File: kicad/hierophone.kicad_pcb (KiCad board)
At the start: 2 copper layers, 220 x 130 mm, 165 parts, among them J1 AudioJack2_SwitchT, J10 Conn_01x02, J2 AudioJack2_SwitchT, J3 Conn_01x03_Pin, J4 AudioJack2_SwitchT, J5 AudioJack2_SwitchT, J6 AudioJack2_SwitchT, J7 AudioJack2_SwitchT, J8 Conn_01x02, J9 Conn_01x02, Q1 2N3904, Q2 2N3906, Q3 2N3906, SW1 SW_SPDT, SW3 SW_SPDT, U10 TL072, U11 TL072, U12 TL072, U13 TL072, U2 LM13700, U3 LM13700, U4 TL072, U5 TL072, U6 LM386, U7 NE5534, U8 TL072, U9 ICL7660

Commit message: Fixing issues with the inputs
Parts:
- removed R18: 47k, Rumblesan_Standard_Parts:R_Axial_DIN0207_L6.3mm_D2.5mm_P10.16mm_Horizontal
- removed U11: TL072, Package_DIP:DIP-8_W7.62mm_Socket
- added C44: 22pF, Rumblesan_Standard_Parts:C_Rect_L7.0mm_W2.5mm_P5.00mm, F.Cu at (76.5, 97.8)
- added R59: 100k, Rumblesan_Standard_Parts:R_Axial_DIN0207_L6.3mm_D2.5mm_P10.16mm_Horizontal, F.Cu at (52.3, 144.8)
- added R60: 100k, Rumblesan_Standard_Parts:R_Axial_DIN0207_L6.3mm_D2.5mm_P10.16mm_Horizontal, F.Cu at (52.6, 129.0)
- added R61: 100k, Rumblesan_Standard_Parts:R_Axial_DIN0207_L6.3mm_D2.5mm_P10.16mm_Horizontal, F.Cu at (91.7, 106.2)
- added R62: 10k, Rumblesan_Standard_Parts:R_Axial_DIN0207_L6.3mm_D2.5mm_P10.16mm_Horizontal, F.Cu at (66.3, 100.8)
- added U1: TL074, Package_DIP:DIP-14_W7.62mm_Socket, F.Cu at (55.4, 112.0)
- R13, R2: value 1k -> 10k
- moved R8 40.8 mm to (44.5, 137.9), turned to 180 degrees
- moved TP4 37.2 mm to (41.1, 100.8)
- moved R7 34.6 mm to (44.5, 134.9), turned to 180 degrees
- moved C33 33.9 mm to (42.9, 90.7), turned to 0 degrees
- moved C35 30.8 mm to (46.0, 97.5), turned to 0 degrees
- moved R6 27.6 mm to (55.9, 100.8), turned to 180 degrees
- moved J1 25.0 mm to (45.0, 125.0)
- moved J2 25.0 mm to (45.0, 150.0)
- moved RV1 25.0 mm to (70.0, 125.0)
- moved RV2 25.0 mm to (70.0, 150.0)
- moved C32 17.1 mm to (63.0, 115.6)
- moved C36 16.6 mm to (58.7, 100.8), turned to 0 degrees
- moved R51 9.25 mm to (51.3, 92.5), turned to 90 degrees
- moved TP5 3.56 mm to (109.2, 114.6)
- moved R45 3.05 mm to (117.6, 136.4)
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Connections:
- J1 pad T: Net-(J1-PadT) -> Net-(U1A-+)
- J2 pad T: Net-(J2-PadT) -> Net-(U1B-+)
- R8 pad 1: AUDIO_INPUT_2 -> Net-(R8-Pad1)
- RV1 pad 3: Net-(J1-PadT) -> Net-(U1A--)
- RV2 pad 2: Net-(U11A-+) -> Net-(R8-Pad1)
- RV2 pad 3: Net-(J2-PadT) -> AUDIO_INPUT_2
- RV8 pad 2: Net-(U6-+) -> Net-(U6--)
- U6 pad 2: GND -> Net-(U6--)
- U6 pad 3: Net-(U6-+) -> GND
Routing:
- net Net-(U1B-+): track 0.00 -> 83.0 mm
- net Net-(U1D--): track 34.2 -> 95.1 mm
- net Net-(C44-Pad1): track 8.00 -> 61.9 mm
- net Net-(R8-Pad1): track 0.00 -> 38.3 mm
- net AUDIO_INPUT_2: track 140.3 -> 178.1 mm, vias 0 -> 1
- net Net-(U1A--): track 0.00 -> 33.1 mm
- net Net-(U1C--): track 0.00 -> 32.5 mm
- net Net-(J2-PadT): track 32.4 -> 0.00 mm
- net Net-(J1-PadT): track 30.4 -> 0.00 mm
- net Net-(U1A-+): track 0.00 -> 28.4 mm
- net Net-(U11A-+): track 25.1 -> 0.00 mm
- net Net-(C4-Pad2): track 11.7 -> 33.5 mm
- net VEE: track 508.8 -> 523.8 mm
- net VCC: track 612.1 -> 626.2 mm
- net Net-(U6-+): track 13.5 -> 0.00 mm
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
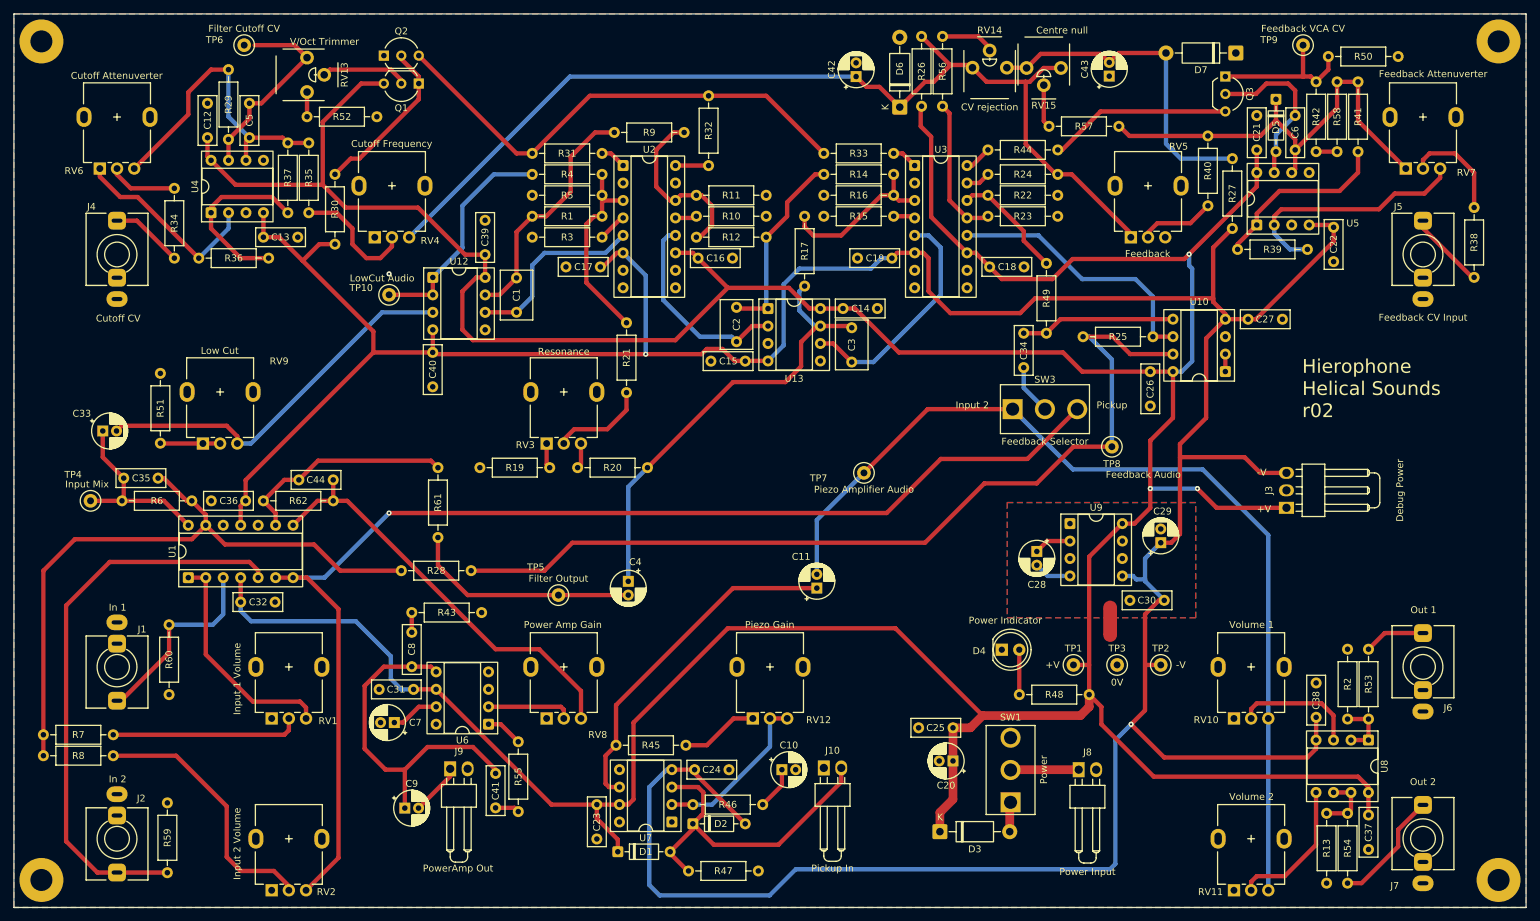
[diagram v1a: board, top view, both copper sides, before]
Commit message: Adding volt per octave input
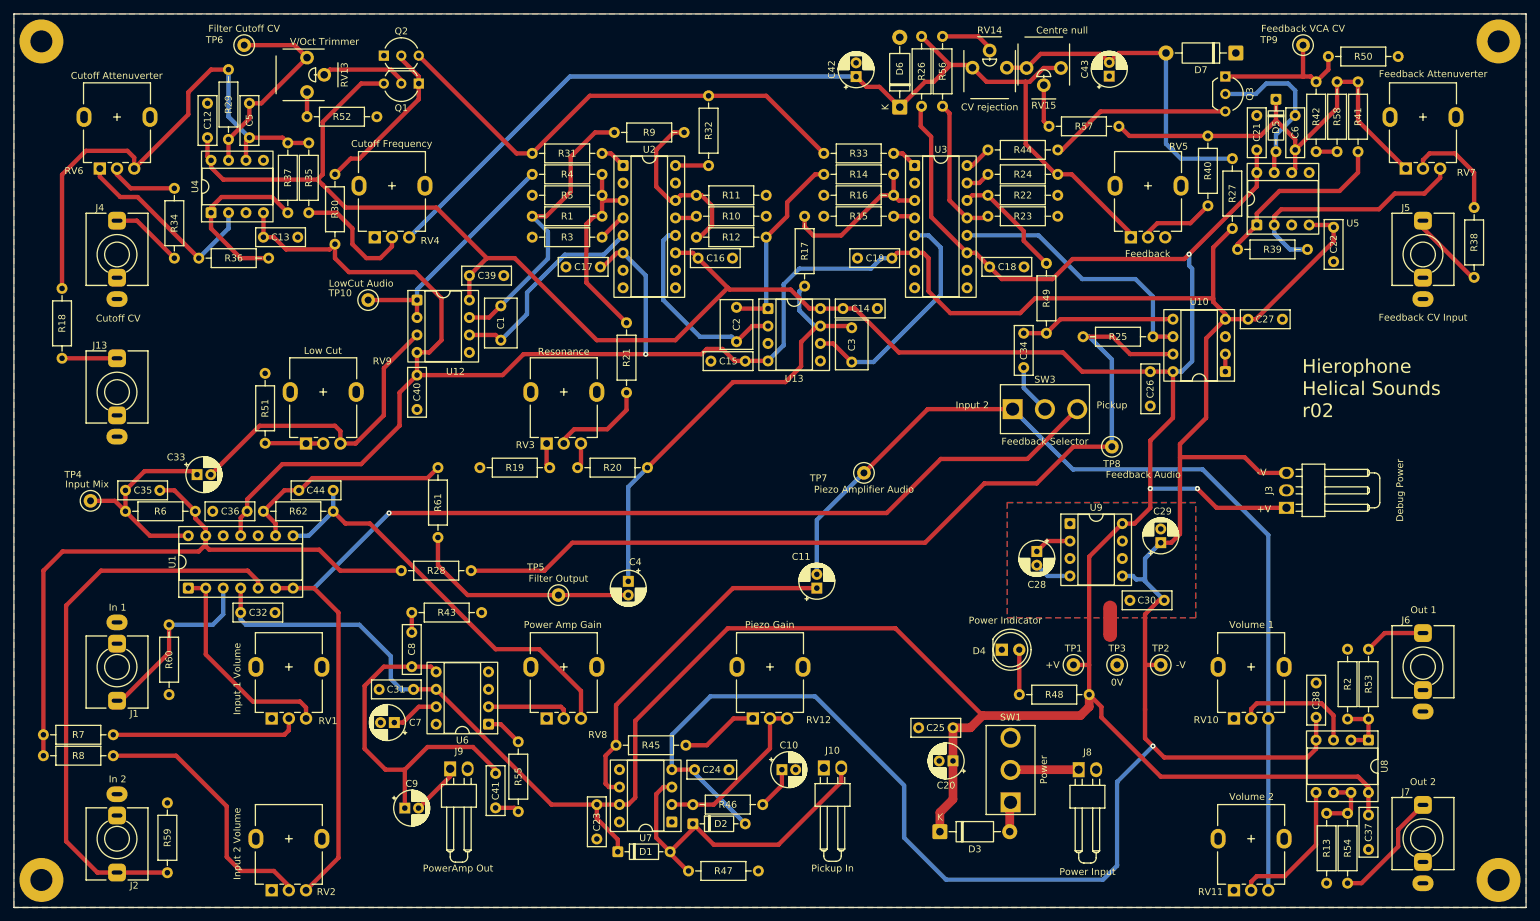
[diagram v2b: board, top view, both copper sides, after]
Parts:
- added J13: AudioJack2_SwitchT, Rumblesan_Audio_Connectors:Jack_3.5mm_QingPu_WQP-PJ398SM_Vertical, F.Cu at (45.0, 85.0)
- added R18: 100k, Rumblesan_Standard_Parts:R_Axial_DIN0207_L6.3mm_D2.5mm_P10.16mm_Horizontal, F.Cu at (37.0, 80.1)
- moved R51 15.2 mm to (66.5, 92.5)
- moved C33 15.1 mm to (56.6, 97.0)
- moved RV9 15.0 mm to (75.0, 85.0)
- moved C1 4.66 mm to (100.8, 72.5)
- moved C40 4.02 mm to (88.6, 87.5)
- moved U12 4.01 mm to (88.6, 71.6)
- moved C39 3.81 mm to (96.3, 68.1), turned to 0 degrees
- moved TP10 3.14 mm to (81.5, 71.6)
- moved C35 1.80 mm to (46.2, 99.3)
- moved R6 1.61 mm to (56.4, 102.4)
- moved C36 1.54 mm to (58.9, 102.4)
- moved C32 1.52 mm to (63.0, 117.1)
- moved R62 1.52 mm to (66.3, 102.4)
- moved U1 1.52 mm to (55.4, 113.5)
- moved C44 1.52 mm to (76.5, 99.3)
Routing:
- net Net-(U4B--): track 45.2 -> 75.7 mm
- net Net-(U12A-+): track 55.9 -> 45.6 mm
- net VEE: track 523.8 -> 534.1 mm
- net Net-(J13-PadT): track 0.00 -> 8.00 mm
- net Net-(C1-Pad1): track 35.5 -> 42.1 mm
- net VCC: track 626.2 -> 620.3 mm
- net Net-(C33-Pad1): track 27.2 -> 31.2 mm
- net Net-(U12B--): track 27.4 -> 30.8 mm
- net Net-(U12A--): track 33.2 -> 34.9 mm
- net Net-(D1-A): track 48.2 -> 49.9 mm
- net Net-(U1A-+): track 28.4 -> 26.9 mm
- net Net-(C5-Pad2): track 29.1 -> 30.6 mm
- net Net-(U1A--): track 33.1 -> 31.6 mm
- net Net-(C44-Pad1): track 61.9 -> 61.2 mm
- net GND: vias 1 -> 0

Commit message: More pcb tweaks
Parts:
- moved TP5 15.5 mm to (102.1, 100.8), turned to 180 degrees
- moved C4 14.6 mm to (110.7, 100.8), turned to 180 degrees
- moved R61 7.03 mm to (96.3, 100.8), turned to 180 degrees
- moved R36 6.84 mm to (58.7, 72.1), turned to 90 degrees
- moved R62 1.78 mm to (68.1, 102.4)
- moved R28 1.52 mm to (84.8, 111.0)
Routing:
- net Net-(C4-Pad2): track 33.5 -> 12.5 mm
- net Net-(R36-Pad2): track 26.0 -> 16.6 mm
- net Net-(U4A--): track 28.9 -> 37.2 mm
- net Net-(U1C--): track 32.3 -> 26.0 mm
- net Net-(C3-Pad1): track 66.0 -> 61.7 mm
- net VEE: track 534.1 -> 536.7 mm
- net Net-(R25-Pad2): track 133.1 -> 134.6 mm
- net Net-(U1D--): track 95.4 -> 93.9 mm
- net Net-(C44-Pad1): track 61.2 -> 62.0 mm

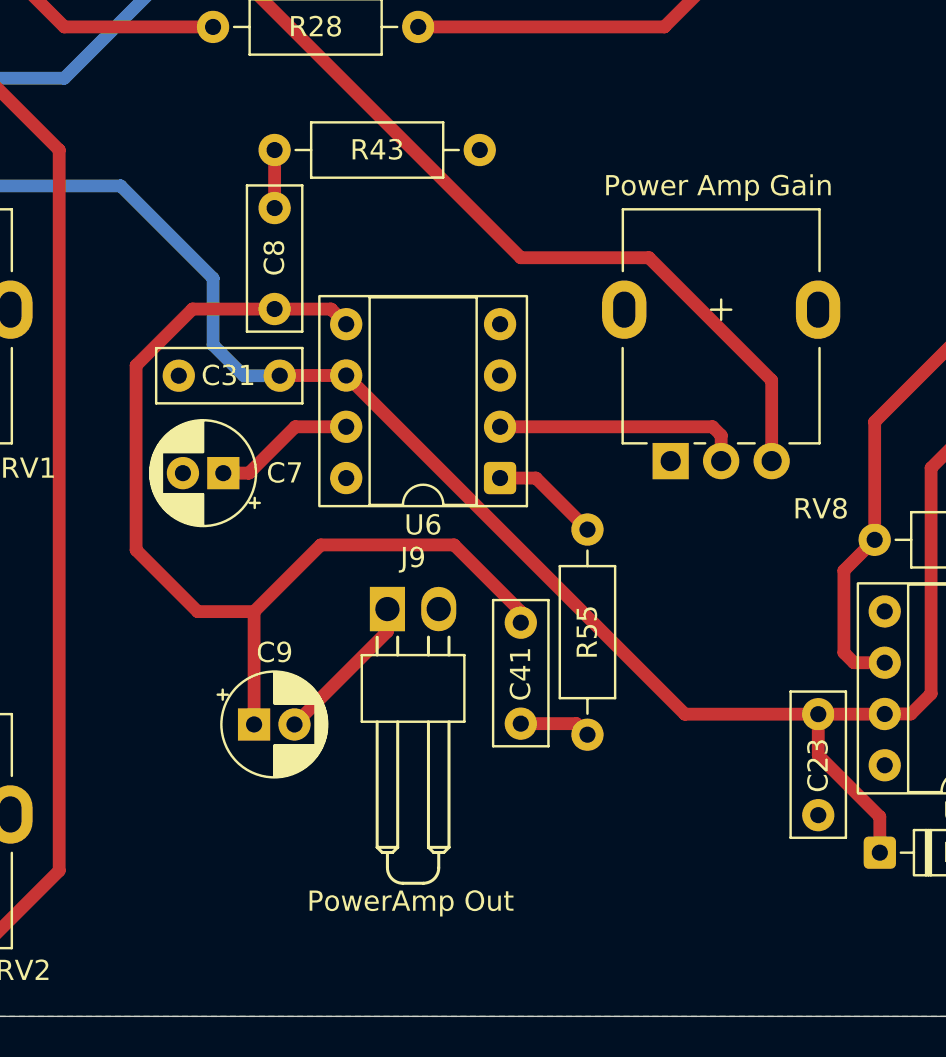
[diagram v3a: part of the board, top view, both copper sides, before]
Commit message: Redesign panel and PCB to have heat vents for power amp
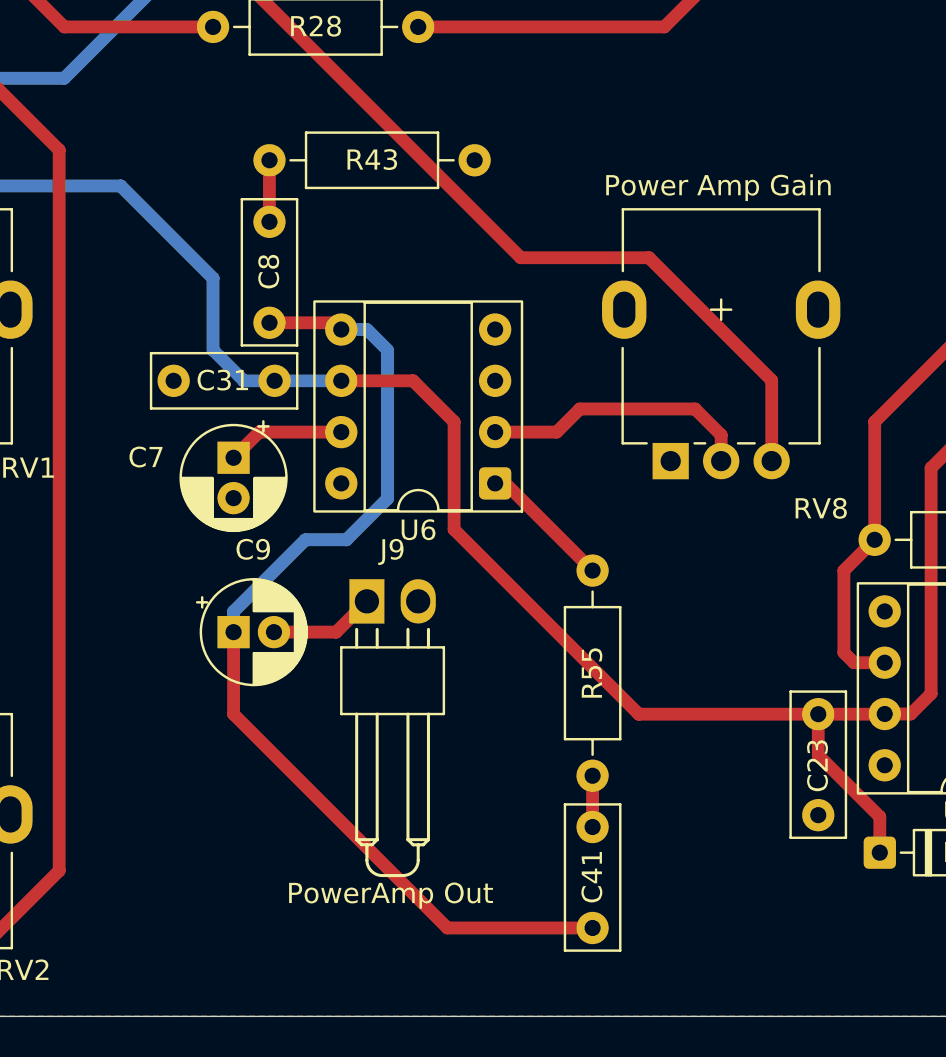
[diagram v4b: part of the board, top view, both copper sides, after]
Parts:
- moved C41 15.5 mm to (103.6, 155.6), turned to 90 degrees
- moved C9 4.68 mm to (85.9, 141.0)
- moved R55 2.05 mm to (103.6, 137.9)
- moved J9 1.09 mm to (92.5, 139.4)
- moved C7 0.92 mm to (85.9, 132.3), turned to -90 degrees
- moved C8 0.73 mm to (87.6, 125.7)
- moved R43 0.57 mm to (87.6, 117.6)
- moved U6 0.36 mm to (98.8, 133.6)
- moved C31 0.36 mm to (87.9, 128.5)
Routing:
- net VCC: track 620.3 -> 623.6 mm
- net Net-(J9-Pin_1): track 7.62 -> 5.24 mm
- net Net-(R55-Pad1): track 5.38 -> 6.61 mm
- net Net-(U6-BYPASS): track 7.04 -> 5.86 mm
- net Net-(U6--): track 12.4 -> 13.5 mm
- net Net-(C41-Pad2): track 3.53 -> 2.54 mm
- net Net-(C41-Pad1): track 50.2 -> 50.9 mm
